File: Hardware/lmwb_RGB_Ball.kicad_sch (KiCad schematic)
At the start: 30 parts, among them J1 Barrel_Jack_MountingPin, U1 24C02S, U2 AMS1117-3.3, U3 STM32C011F6P6

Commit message: did some routing
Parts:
- removed C13: 1u, Capacitor_SMD:C_0805_2012Metric, symbol Device:C
- removed J1: Barrel_Jack_MountingPin, Connector_BarrelJack:BarrelJack_Wuerth_694102107102_1.0x3.9mm, symbol Connector:Barrel_Jack_MountingPin
- added C16: 22u, Capacitor_SMD:C_0805_2012Metric, symbol Device:C
- added C19, C7, C8, C9: 100n, Capacitor_SMD:C_0805_2012Metric, symbol Device:C
- added D2: US1D, Diode_SMD:D_SMA, symbol Diode:US1D
- added H1, H2: MountingHole_Pad, MountingHole:MountingHole_4.3mm_M4_Pad, symbol Mechanical:MountingHole_Pad
- added J1, J2: Conn_01x03, Connector_PinHeader_2.54mm:PinHeader_1x03_P2.54mm_Vertical, symbol Connector_Generic:Conn_01x03
- added R1, R2, R3: 10k, Resistor_SMD:R_0805_2012Metric, symbol Device:R
- renumbered C6 to C1, C3 to C10, C5 to C11, C7 to C12, C4 to C13, C9 to C14, C12 to C15, C14 to C17, C15 to C18, C8 to C2, C1 to C3, C10 to C4, C11 to C5, C2 to C6, D2 to D3, D3 to D4, D4 to D5, D5 to D6, D6 to D7, D7 to D8, D8 to D9, J2 to J3, R1 to R4, U2 to U1, U1 to U2
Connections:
- net +3V3: now also J3.4, C16.1, R1.2, R2.2, R3.2
- net GND: now also J3.1, C16.2, C19.2, C7.2, C8.2, C9.2, H2.1, J2.3 (Pin_3)
- net VCC: now also D2.1 (K)
- net TIM1-CH1: now reaches JP1.1 (A)
- net TIM1-CH1: now also U3.15 (PA8)
- net SPI-MOSI: now reaches JP1.3 (B)
- net SPI-MOSI: now also U3.17 (PA12)
- net SW-CLK: now reaches J3.2
- net SW-CLK: now also U3.19 (PA14)
- net SW-DIO: now reaches J3.3
- net SW-DIO: now also U3.18 (PA13)
- net SCL: now reaches U3.1 (PB7)
- net SCL: now also U2.1 (SCL)
- net EXTI-4: now reaches U3.11 (PA4)
- net EXTI-5: now reaches U3.12 (PA5)
- net EXTI-6: now reaches U3.13 (PA6)
- net SDA: now reaches U3.2 (PC14)
- net SDA: now also U2.3 (SDA)
- net SPI-SCK: now reaches U3.20 (PB6)
- net nRST: now reaches U3.6 (PF2)
- net nRST: now also C19.1
- net UART-TX: now reaches U3.7 (PA0)
- net UART-TX: now also J2.1 (Pin_1)
- net UART-RX: now reaches U3.8 (PA1)
- net UART-RX: now also J2.2 (Pin_2)
- new net: C7.1, J1.1 (Pin_1), R1.1
- new net: C9.1, J1.3 (Pin_3), R3.1
- new net: D2.2 (A), H1.1
- new net: C8.1, J1.2 (Pin_2), R2.1
- no-connect marks 1 -> 6
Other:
- note added: "Extended C16214 Extended C113716 SMD 2.5mm Extended C707276 SMD 2.0mm https://jlcpcb.com/parts/2nd/Connectors/DC_Power_Connectors_3059 package type SMD, inside contact diameter 2mm https://jlcpcb.com/parts/1st/Diodes_4 basic SM4007PL, C64898, SOT123FL"
- note added: "RST-PIN?"
- moved on the sheet: C1, C13, C2, C4, C5, J3, R4, U1, U2

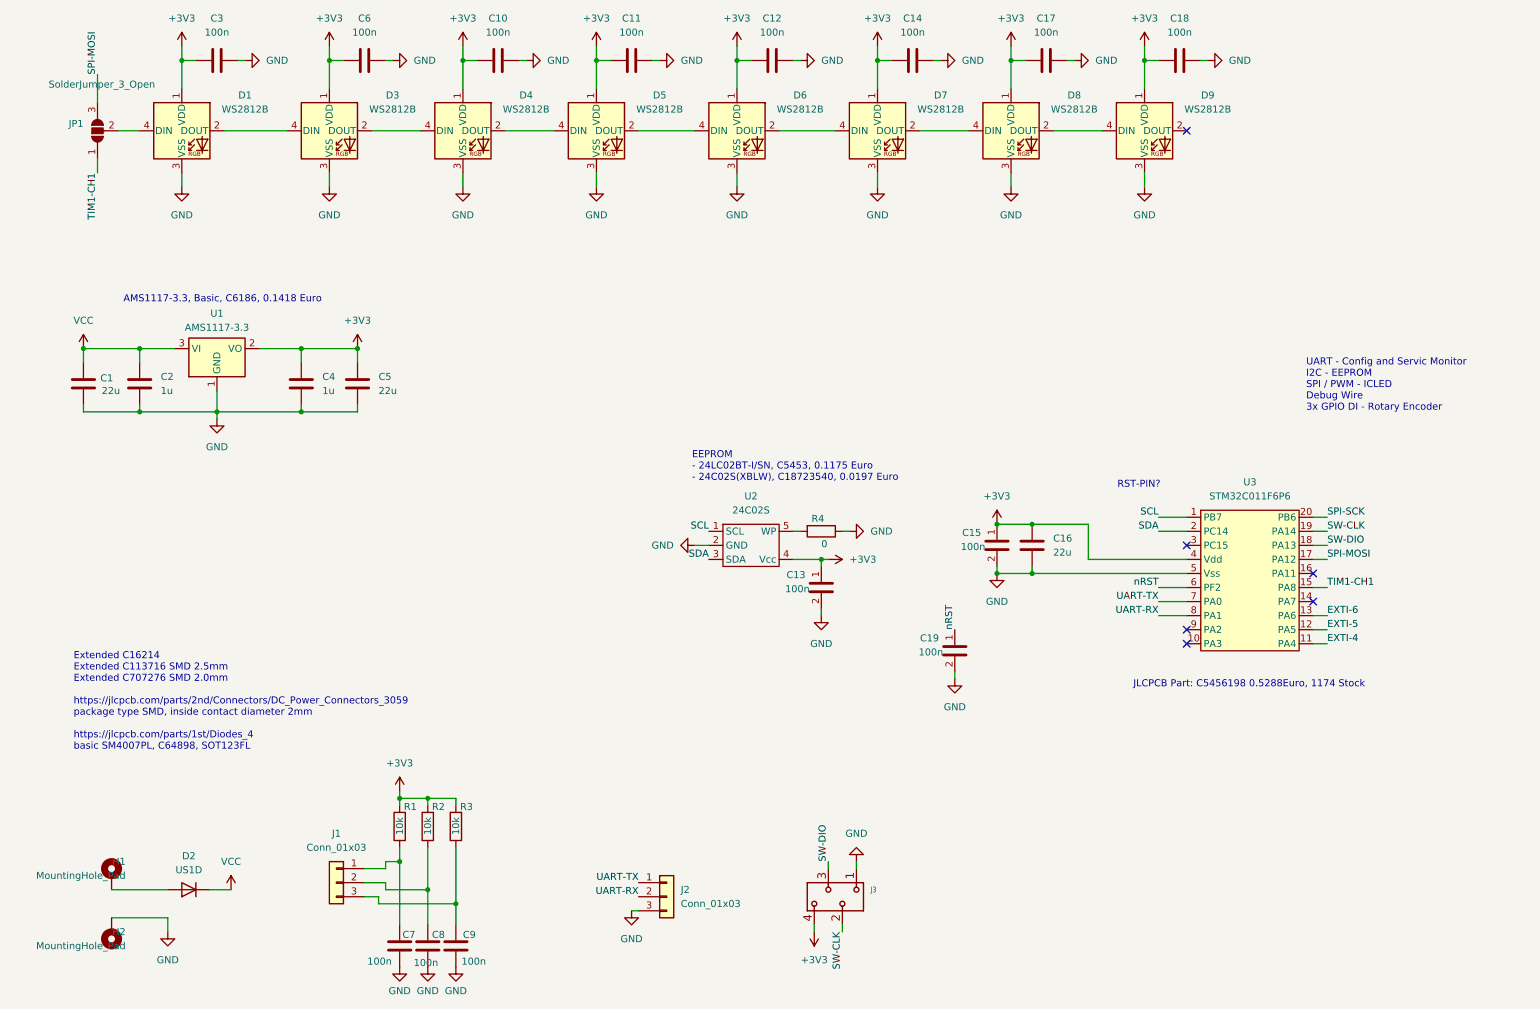
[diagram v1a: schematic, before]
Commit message: added F04xx project, coded firmware, progress on layout
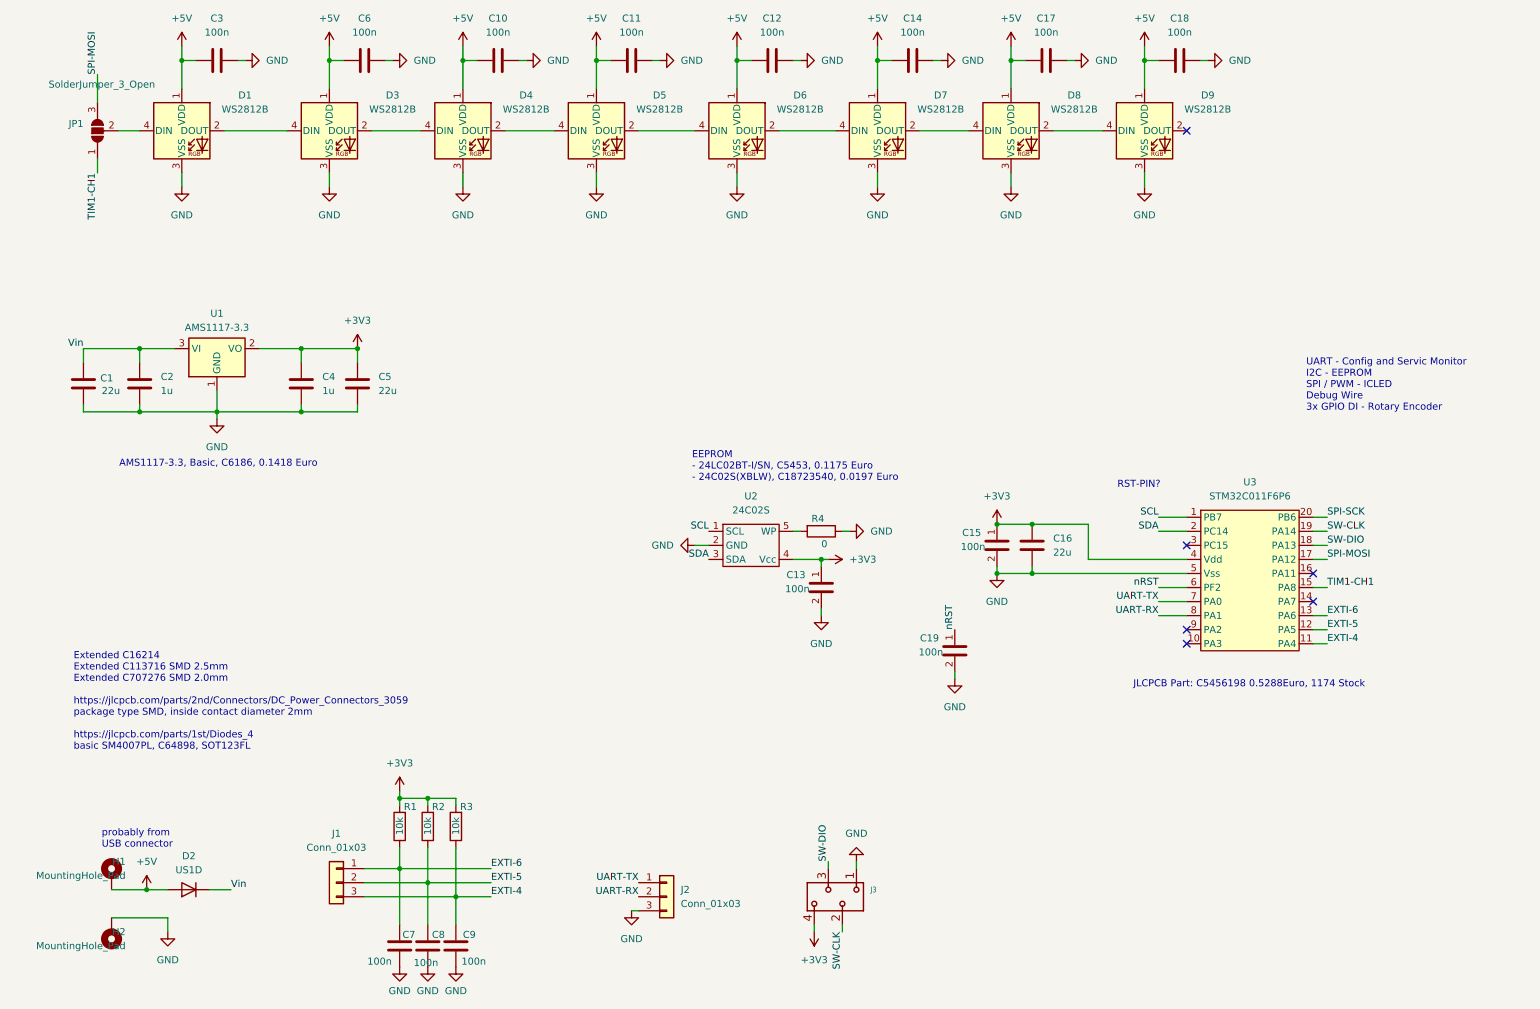
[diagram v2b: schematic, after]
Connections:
- net +3V3: no longer C10.1, C11.1, C12.1, C14.1, C17.1, C18.1, C3.1, C6.1, D1.1 (VDD), D3.1 (VDD), D4.1 (VDD), D5.1 (VDD), D6.1 (VDD), D7.1 (VDD), D8.1 (VDD), D9.1 (VDD)
- net EXTI-4: now also C9.1, J1.3 (Pin_3), R3.1
- net EXTI-5: now also C8.1, J1.2 (Pin_2), R2.1
- net EXTI-6: now also C7.1, J1.1 (Pin_1), R1.1
- net +5V: now reaches D2.2 (A), H1.1
- net +5V: now also C10.1, C11.1, C12.1, C14.1, C17.1, C18.1, C3.1, C6.1, D1.1 (VDD), D3.1 (VDD), D4.1 (VDD), D5.1 (VDD), D6.1 (VDD), D7.1 (VDD), D8.1 (VDD), D9.1 (VDD)
- net VCC renamed Vin
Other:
- note added: "probably from USB connector"

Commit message: progress on layout
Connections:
- net UART-RX: now also J2.1 (Pin_1); no longer J2.2 (Pin_2)
- net UART-TX: now also J2.2 (Pin_2); no longer J2.1 (Pin_1)
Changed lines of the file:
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@@
 	)
 	(label "UART-RX"
-		(at 120.65 177.8 180)
+		(at 120.65 175.26 180)
 		(effects
 			(font
@@
 	)
 	(label "UART-TX"
-		(at 120.65 175.26 180)
+		(at 120.65 177.8 180)
 		(effects
 			(font

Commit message: order pcb and assambly
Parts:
- C7, C8, C9: LCSC PN (none) -> C49678
- D1, D3, D4, D5, D6, D7, D8, D9: LCSC PN (none) -> C2761795; now not fitted
- H1, H2, J1, J2, J3, JP1: now not fitted
- R1, R2, R3: LCSC PN (none) -> C17414
- U1: LCSC PN (none) -> C6186
- U2: LCSC PN (none) -> C18723540
- U3: LCSC PN (none) -> C5456198
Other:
- note added: "C4154882_ C2761795_SMD5050-P4 -> passt das? yes, a "SMD 5050-p4" footprint is essentially the same as a "PLC4 5050" footprint"
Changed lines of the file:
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@@
 		)
 	)
+	(text "C4154882_\nC2761795_SMD5050-P4 -> passt das?\nyes, a \"SMD 5050-p4\" footprint is essentially\nthe same as a \"PLC4 5050\" footprint "
+		(exclude_from_sim no)
+		(at 61.468 61.722 0)
+		(effects
+			(font
+				(size 1.27 1.27)
+			)
+		)
+	)
 	(junction
 		(at 82.55 175.26)
@@
 		(in_bom yes)
 		(on_board yes)
-		(dnp no)
+		(dnp yes)
 		(fields_autoplaced yes)
 		(property "Reference" "D8"
@@
 			)
 		)
+		(property "LCSC PN" "C2761795"
+			(at 187.96 39.37 0)
+			(effects
+				(font
+					(size 1.27 1.27)
+				)
+				(hide yes)
+			)
+		)
 		(pin "2"
 		)
@@
 		(in_bom no)
 		(on_board yes)
-		(dnp no)
+		(dnp yes)
 		(property "Reference" "H2"
 			(at 27.94 184.1499 0)
@@
 			)
 		)
+		(property "LCSC PN" "C17414"
+			(at 77.47 165.1 0)
+			(effects
+				(font
+					(size 1.27 1.27)
+				)
+				(hide yes)
+			)
+		)
 		(pin "2"
 		)
@@
 		(in_bom yes)
 		(on_board yes)
-		(dnp no)
+		(dnp yes)
 		(fields_autoplaced yes)
 		(property "Reference" "J2"
@@
 			)
 		)
+		(property "LCSC PN" "C17414"
+			(at 87.63 165.1 0)
+			(effects
+				(font
+					(size 1.27 1.27)
+				)
+				(hide yes)
+			)
+		)
 		(pin "2"
 		)
@@
 		(in_bom yes)
 		(on_board yes)
-		(dnp no)
+		(dnp yes)
 		(fields_autoplaced yes)
 		(property "Reference" "D1"
@@
 			)
 		)
+		(property "LCSC PN" "C2761795"
+			(at 38.1 39.37 0)
+			(effects
+				(font
+					(size 1.27 1.27)
+				)
+				(hide yes)
+			)
+		)
 		(pin "2"
 		)
@@
 		(in_bom no)
 		(on_board yes)
-		(dnp no)
+		(dnp yes)
 		(property "Reference" "JP1"
 			(at 20.32 38.0999 90)
@@
 			)
 		)
+		(property "LCSC PN" "C49678"
+			(at 77.47 186.69 0)
+			(effects
+				(font
+					(size 1.27 1.27)
+				)
+				(hide yes)
+			)
+		)
 		(pin "1"
 		)
@@
 		(in_bom yes)
 		(on_board yes)
-		(dnp no)
+		(dnp yes)
 		(fields_autoplaced yes)
 		(property "Reference" "D5"
@@
 			)
 		)
+		(property "LCSC PN" "C2761795"
+			(at 113.03 39.37 0)
+			(effects
+				(font
+					(size 1.27 1.27)
+				)
+				(hide yes)
+			)
+		)
 		(pin "2"
 		)
@@
 		(in_bom yes)
 		(on_board yes)
-		(dnp no)
+		(dnp yes)
 		(fields_autoplaced yes)
 		(property "Reference" "D6"
@@
 			)
 		)
+		(property "LCSC PN" "C2761795"
+			(at 138.43 39.37 0)
+			(effects
+				(font
+					(size 1.27 1.27)
+				)
+				(hide yes)
+			)
+		)
 		(pin "2"
 		)
@@
 			)
 		)
+		(property "LCSC PN" "C17414"
+			(at 82.55 165.1 0)
+			(effects
+				(font
+					(size 1.27 1.27)
+				)
+				(hide yes)
+			)
+		)
 		(pin "2"
 		)
@@
 		(in_bom yes)
 		(on_board yes)
-		(dnp no)
+		(dnp yes)
 		(fields_autoplaced yes)
 		(property "Reference" "J1"
@@
 		(in_bom yes)
 		(on_board yes)
-		(dnp no)
+		(dnp yes)
 		(fields_autoplaced yes)
 		(property "Reference" "D7"
@@
 			)
 		)
+		(property "LCSC PN" "C2761795"
+			(at 163.83 39.37 0)
+			(effects
+				(font
+					(size 1.27 1.27)
+				)
+				(hide yes)
+			)
+		)
 		(pin "2"
 		)
@@
 		(in_bom yes)
 		(on_board yes)
-		(dnp no)
+		(dnp yes)
 		(fields_autoplaced yes)
 		(property "Reference" "D9"
@@
 			)
 		)
+		(property "LCSC PN" "C2761795"
+			(at 212.09 39.37 0)
+			(effects
+				(font
+					(size 1.27 1.27)
+				)
+				(hide yes)
+			)
+		)
 		(pin "2"
 		)
@@
 			)
 		)
+		(property "LCSC PN" "C49678"
+			(at 82.55 186.69 0)
+			(effects
+				(font
+					(size 1.27 1.27)
+				)
+				(hide yes)
+			)
+		)
 		(pin "1"
 		)
@@
 		(in_bom no)
 		(on_board yes)
-		(dnp no)
+		(dnp yes)
 		(property "Reference" "H1"
 			(at 27.94 171.4499 0)
@@
 		(in_bom yes)
 		(on_board yes)
-		(dnp no)
+		(dnp yes)
 		(fields_autoplaced yes)
 		(property "Reference" "J3"
@@
 		(in_bom yes)
 		(on_board yes)
-		(dnp no)
+		(dnp yes)
 		(fields_autoplaced yes)
 		(property "Reference" "D4"
@@
 			)
 		)
+		(property "LCSC PN" "C2761795"
+			(at 88.9 39.37 0)
+			(effects
+				(font
+					(size 1.27 1.27)
+				)
+				(hide yes)
+			)
+		)
 		(pin "2"
 		)
@@
 			)
 		)
+		(property "LCSC PN" "C5456198"
+			(at 219.71 109.22 0)
+			(effects
+				(font
+					(size 1.27 1.27)
+				)
+				(hide yes)
+			)
+		)
 		(pin "12"
 		)
@@
 			)
 		)
+		(property "LCSC PN" "C6186"
+			(at 44.45 78.74 0)
+			(effects
+				(font
+					(size 1.27 1.27)
+				)
+				(hide yes)
+			)
+		)
 		(pin "1"
 		)
@@
 			)
 		)
+		(property "LCSC PN" "C49678"
+			(at 87.63 186.69 0)
+			(effects
+				(font
+					(size 1.27 1.27)
+				)
+				(hide yes)
+			)
+		)
 		(pin "1"
 		)
@@
 		(in_bom yes)
 		(on_board yes)
-		(dnp no)
+		(dnp yes)
 		(fields_autoplaced yes)
 		(property "Reference" "D3"
@@
 			)
 		)
+		(property "LCSC PN" "C2761795"
+			(at 64.77 39.37 0)
+			(effects
+				(font
+					(size 1.27 1.27)
+				)
+				(hide yes)
+			)
+		)
 		(pin "2"
 		)
@@
 			(at 133.35 111.76 0)
 			(effects
+				(font
+					(size 1.27 1.27)
+				)
+				(hide yes)
+			)
+		)
+		(property "LCSC PN" "C18723540"
+			(at 133.35 111.76 0)
+			(effects
